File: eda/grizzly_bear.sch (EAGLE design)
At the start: 60 parts, among them Q1 PSMN4R0, Q2 PSMN4R0, Q3 PSMN4R0, Q4 PSMN4R0, Q5 IPD90P03P4L, U1 A4940, U2 ATMEGA32U4-AU, U3 ACS714, U4 UA78L00, U5 ISL83491SOIC, Y1 16MHz

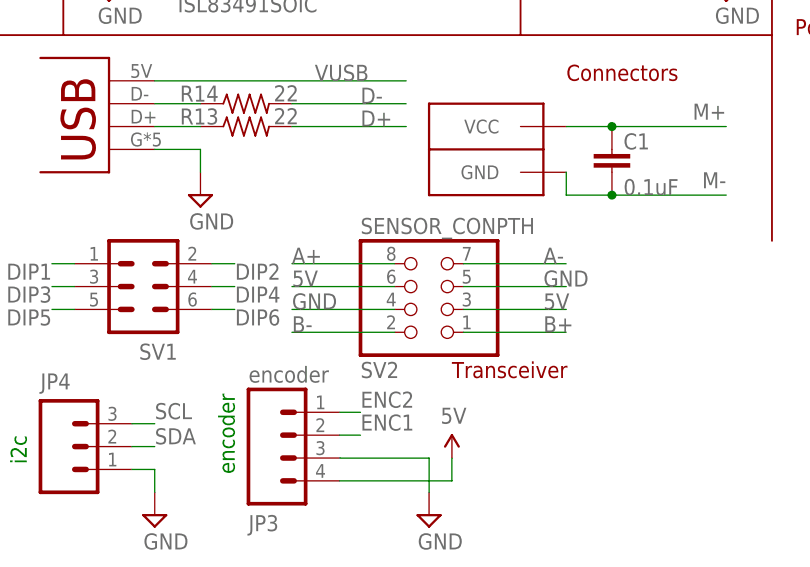
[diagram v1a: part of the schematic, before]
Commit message: Change smartsensor connector to 2x5 on grizzly bear
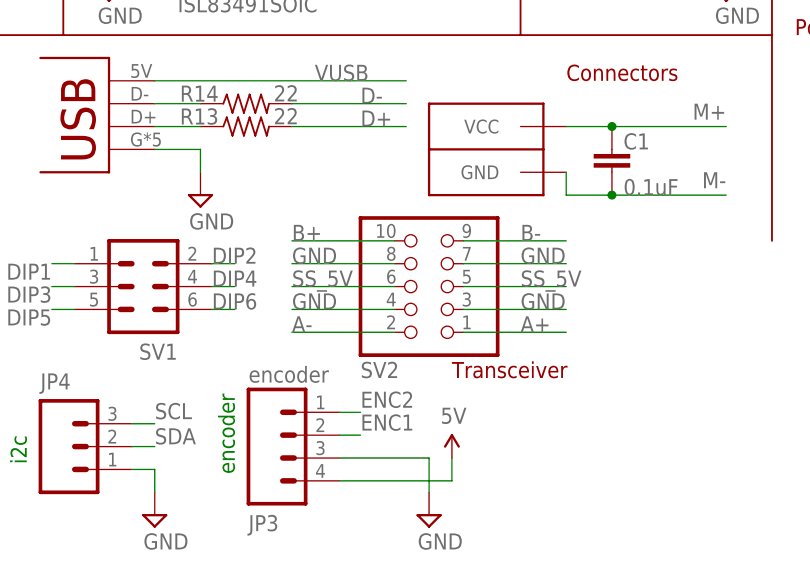
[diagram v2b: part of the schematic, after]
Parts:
- SV2: value SENSOR_CONPTH -> (none); device pie:SENSOR_CONPTH -> pie:SENSOR_CON_5PINPTH
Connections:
- new net SS_5V: SV2.5, SV2.6
- net 5V: no longer SV2.3, SV2.6
- net A+: now also SV2.1; no longer SV2.8
- net A-: now also SV2.2; no longer SV2.7
- net B+: now also SV2.10; no longer SV2.1
- net B-: now also SV2.9; no longer SV2.2
- net GND: now also SV2.3, SV2.7, SV2.8; no longer SV2.5
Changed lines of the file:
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@@
 <part name="SUPPLY9" library="pie" deviceset="GND" device=""/>
 <part name="U$15" library="pie" deviceset="5V" device=""/>
-<part name="SV2" library="pie" deviceset="SENSOR_CON" device="PTH"/>
+<part name="SV2" library="pie" deviceset="SENSOR_CON_5PIN" device="PTH"/>
 <part name="C17" library="pie" deviceset="CAP" device="0603-CAP" value="0.1uF"/>
 </parts>
@@
 <pinref part="U$15" gate="G$1" pin="5V"/>
 </segment>
-<segment>
-<label x="114.3" y="30.48" size="1.778" layer="95"/>
-<pinref part="SV2" gate="G$1" pin="6"/>
-<wire x1="125.73" y1="30.48" x2="114.3" y2="30.48" width="0.1524" layer="91"/>
-</segment>
-<segment>
-<label x="142.24" y="27.94" size="1.778" layer="95"/>
-<pinref part="SV2" gate="G$1" pin="3"/>
-<wire x1="133.35" y1="27.94" x2="144.78" y2="27.94" width="0.1524" layer="91"/>
-</segment>
 </net>
 <net name="CP2" class="0">
@@
 <segment>
 <wire x1="105.41" y1="27.94" x2="107.95" y2="27.94" width="0.1524" layer="91"/>
-<label x="113.03" y="27.94" size="1.778" layer="95" rot="R180"/>
+<label x="105.41" y="27.94" size="1.778" layer="95"/>
 <pinref part="SV1" gate="1" pin="6"/>
 </segment>
@@
 <segment>
 <wire x1="105.41" y1="30.48" x2="107.95" y2="30.48" width="0.1524" layer="91"/>
-<label x="113.03" y="30.48" size="1.778" layer="95" rot="R180"/>
+<label x="105.41" y="30.48" size="1.778" layer="95"/>
 <pinref part="SV1" gate="1" pin="4"/>
 </segment>
@@
 <segment>
 <wire x1="105.41" y1="33.02" x2="107.95" y2="33.02" width="0.1524" layer="91"/>
-<label x="113.03" y="33.02" size="1.778" layer="95" rot="R180"/>
+<label x="105.41" y="33.02" size="1.778" layer="95"/>
 <pinref part="SV1" gate="1" pin="2"/>
 </segment>
@@
 </segment>
 <segment>
-<label x="114.3" y="33.02" size="1.778" layer="95"/>
-<pinref part="SV2" gate="G$1" pin="8"/>
-<wire x1="125.73" y1="33.02" x2="114.3" y2="33.02" width="0.1524" layer="91"/>
+<label x="139.7" y="25.4" size="1.778" layer="95"/>
+<pinref part="SV2" gate="G$1" pin="1"/>
+<wire x1="133.35" y1="25.4" x2="144.78" y2="25.4" width="0.1524" layer="91"/>
 </segment>
 </net>
@@
 </segment>
 <segment>
-<label x="142.24" y="33.02" size="1.778" layer="95"/>
-<pinref part="SV2" gate="G$1" pin="7"/>
-<wire x1="133.35" y1="33.02" x2="144.78" y2="33.02" width="0.1524" layer="91"/>
+<label x="114.3" y="25.4" size="1.778" layer="95"/>
+<pinref part="SV2" gate="G$1" pin="2"/>
+<wire x1="125.73" y1="25.4" x2="114.3" y2="25.4" width="0.1524" layer="91"/>
 </segment>
 </net>
@@
 </segment>
 <segment>
-<label x="142.24" y="25.4" size="1.778" layer="95"/>
-<pinref part="SV2" gate="G$1" pin="1"/>
-<wire x1="133.35" y1="25.4" x2="144.78" y2="25.4" width="0.1524" layer="91"/>
+<label x="114.3" y="35.56" size="1.778" layer="95"/>
+<pinref part="SV2" gate="G$1" pin="10"/>
+<wire x1="114.3" y1="35.56" x2="125.73" y2="35.56" width="0.1524" layer="91"/>
 </segment>
 </net>
@@
 </segment>
 <segment>
-<label x="142.24" y="30.48" size="1.778" layer="95"/>
-<pinref part="SV2" gate="G$1" pin="5"/>
-<wire x1="133.35" y1="30.48" x2="144.78" y2="30.48" width="0.1524" layer="91"/>
-</segment>
-<segment>
 <label x="114.3" y="27.94" size="1.778" layer="95"/>
 <pinref part="SV2" gate="G$1" pin="4"/>
 <wire x1="125.73" y1="27.94" x2="114.3" y2="27.94" width="0.1524" layer="91"/>
+<label x="114.3" y="33.02" size="1.778" layer="95"/>
 </segment>
 <segment>
@@
 <wire x1="10.16" y1="124.46" x2="10.16" y2="116.84" width="0.1524" layer="91"/>
 </segment>
+<segment>
+<label x="139.7" y="33.02" size="1.778" layer="95"/>
+<label x="139.7" y="27.94" size="1.778" layer="95"/>
+<pinref part="SV2" gate="G$1" pin="7"/>
+<wire x1="133.35" y1="33.02" x2="144.78" y2="33.02" width="0.1524" layer="91"/>
+</segment>
+<segment>
+<wire x1="133.35" y1="27.94" x2="144.78" y2="27.94" width="0.1524" layer="91"/>
+<pinref part="SV2" gate="G$1" pin="3"/>
+</segment>
+<segment>
+<wire x1="125.73" y1="33.02" x2="114.3" y2="33.02" width="0.1524" layer="91"/>
+<pinref part="SV2" gate="G$1" pin="8"/>
+</segment>
 </net>
 <net name="RXD1" class="0">
@@
 </segment>
 <segment>
-<label x="114.3" y="25.4" size="1.778" layer="95"/>
-<pinref part="SV2" gate="G$1" pin="2"/>
-<wire x1="125.73" y1="25.4" x2="114.3" y2="25.4" width="0.1524" layer="91"/>
-</segment>
-</net>
+<label x="139.7" y="35.56" size="1.778" layer="95"/>
+<wire x1="133.35" y1="35.56" x2="144.78" y2="35.56" width="0.1524" layer="91"/>
+<pinref part="SV2" gate="G$1" pin="9"/>
+</segment>
+</net>
+<net name="SS_5V" class="0">
+<segment>
+<label x="139.7" y="30.48" size="1.778" layer="95"/>
+<wire x1="133.35" y1="30.48" x2="144.78" y2="30.48" width="0.1524" layer="91"/>
+<pinref part="SV2" gate="G$1" pin="5"/>
+</segment>
+<segment>
+<label x="114.3" y="30.48" size="1.778" layer="95"/>
+<pinref part="SV2" gate="G$1" pin="6"/>
+<wire x1="125.73" y1="30.48" x2="114.3" y2="30.48" width="0.1524" layer="91"/>
+</segment>
+</net>
